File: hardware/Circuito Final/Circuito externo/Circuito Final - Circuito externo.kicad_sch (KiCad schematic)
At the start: 26 parts, among them J1 Conn_02x19_Odd_Even, J2 Conn_02x19_Odd_Even, J3 Conn_01x02, J4 Conn_01x02, SW1 SW_SPDT, SW2 SW_DIP_x04, U1 Opamp_Quad, U2 Opamp_Dual

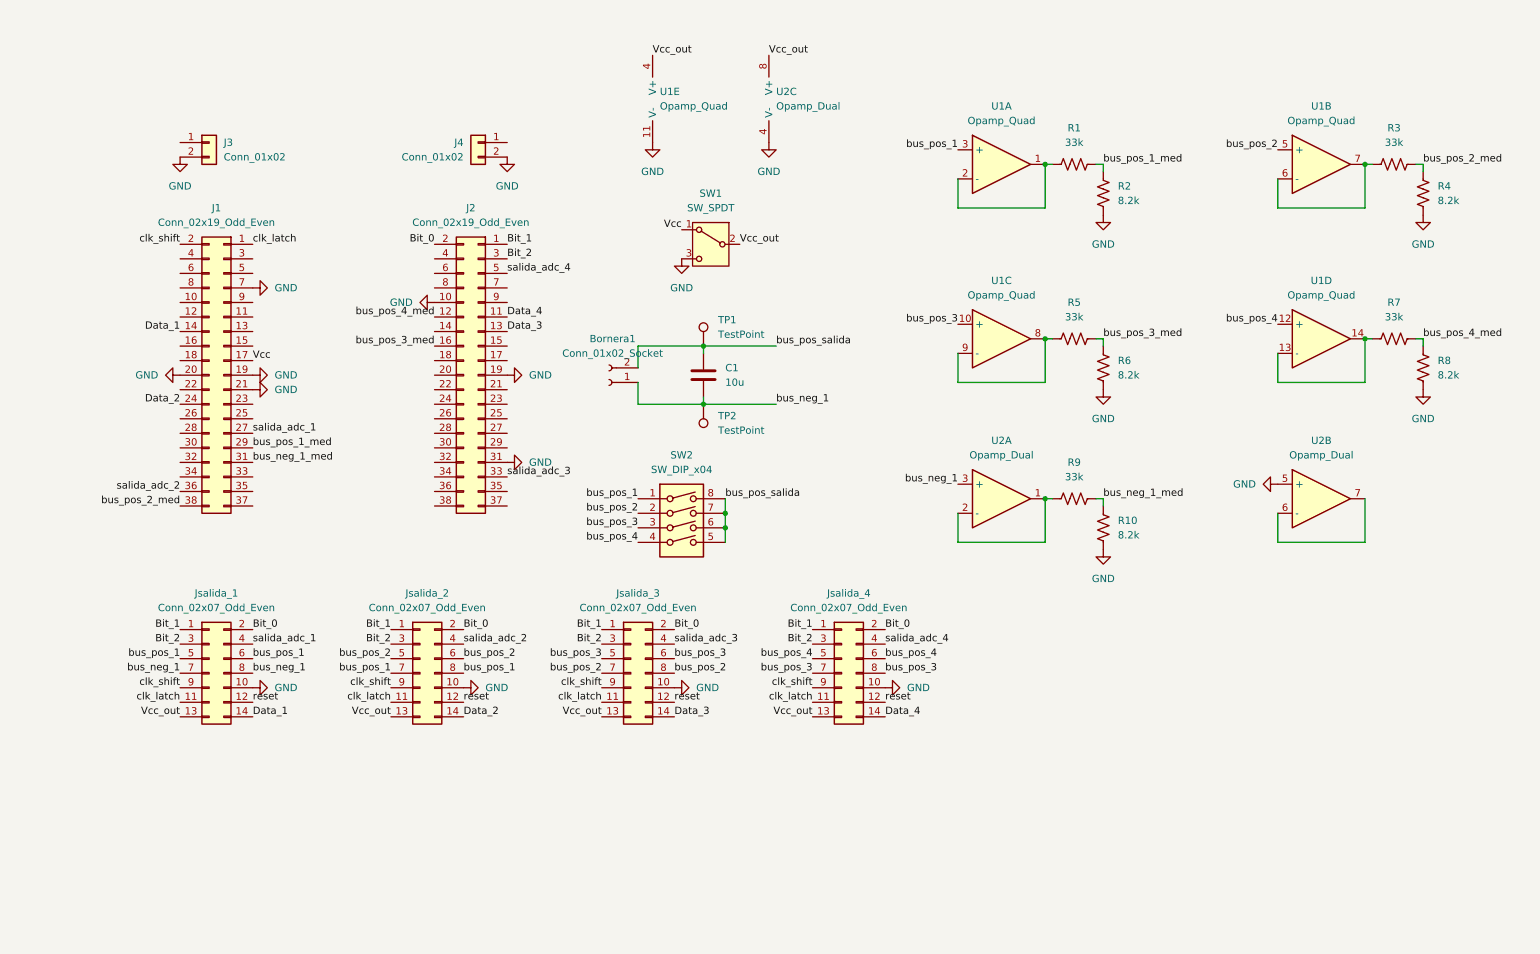
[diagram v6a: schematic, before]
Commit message: subida de la bitacora, del spice del sumador no inversor y update del kicad del circuito central
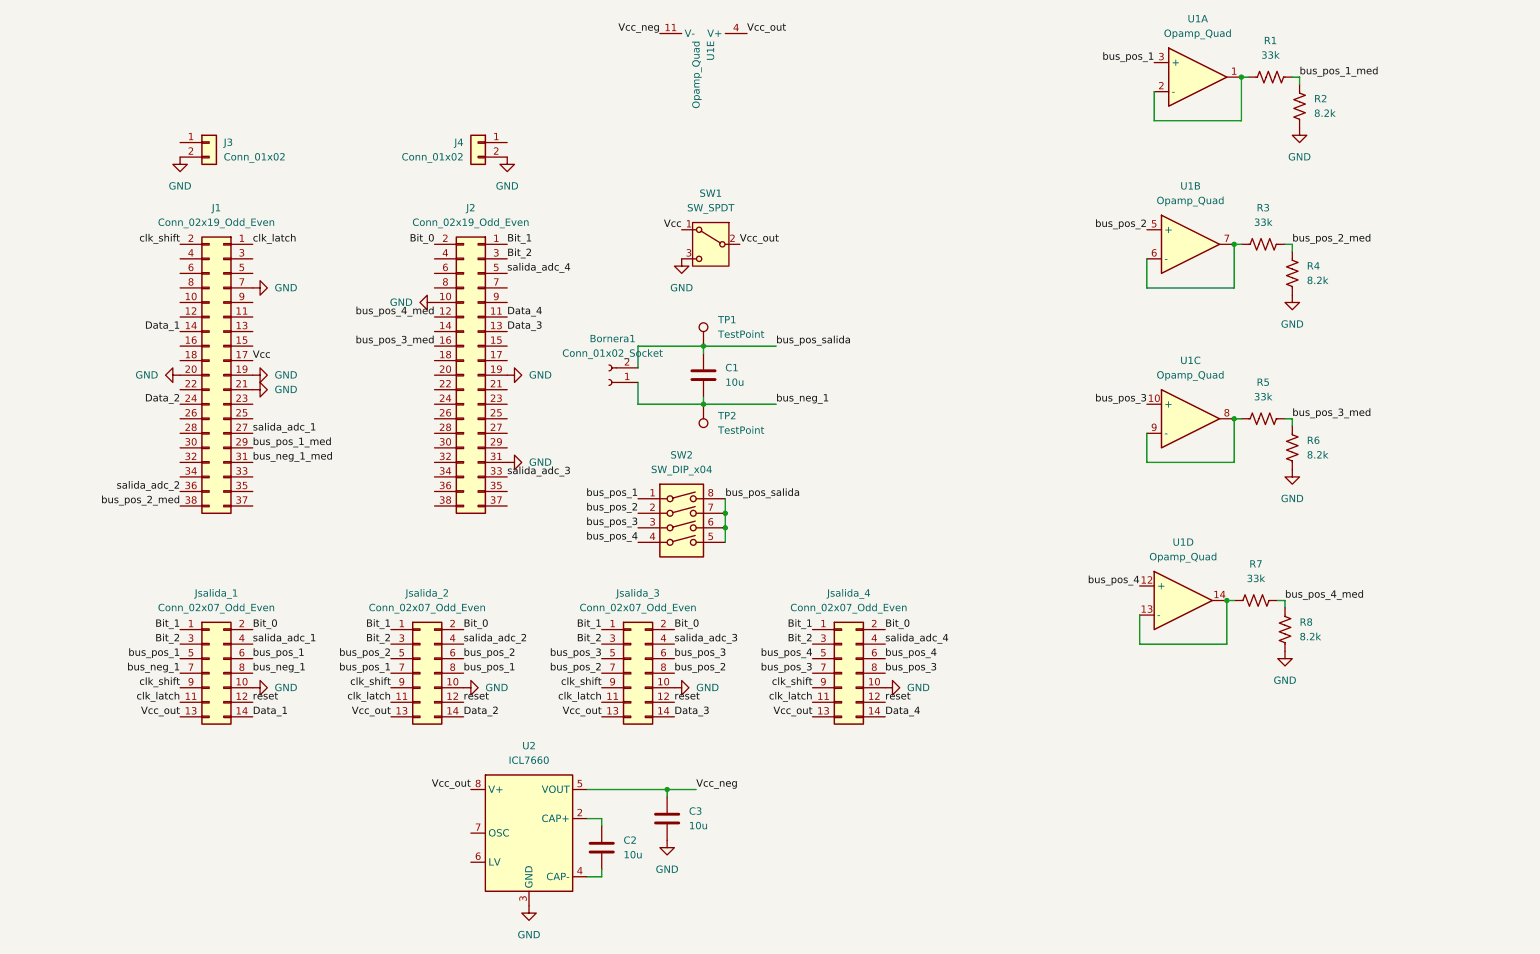
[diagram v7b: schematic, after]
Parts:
- removed R10: 8.2k, symbol Device:R_US
- removed R9: 33k, symbol Device:R_US
- removed U2: Opamp_Dual, symbol Device:Opamp_Dual
- added C2, C3: 10u, Capacitor_SMD:C_1206_3216Metric_Pad1.33x1.80mm_HandSolder, symbol Device:C
- added U2: ICL7660, Package_SO:SOIC-8_3.9x4.9mm_P1.27mm, symbol Regulator_SwitchedCapacitor:ICL7660
- R1, R2: footprint (none) -> Resistor_SMD:R_1206_3216Metric_Pad1.30x1.75mm_HandSolder
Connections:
- net GND: now also C3.2, U2.3 (GND); no longer U1.11 (V-)
- net Vcc_out: now also U2.8 (V+)
- new net: C2.1, U2.2 (CAP+)
- new net: C2.2, U2.4 (CAP-)
- new net Vcc_neg: C3.1, U1.11 (V-), U2.5 (VOUT)
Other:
- moved on the sheet: R1, R2, R3, R4, R5, R6, R7, R8, U1A, U1B, U1C, U1D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

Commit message: update del pcb del circuito central y subida de bitacora del 24 de junio
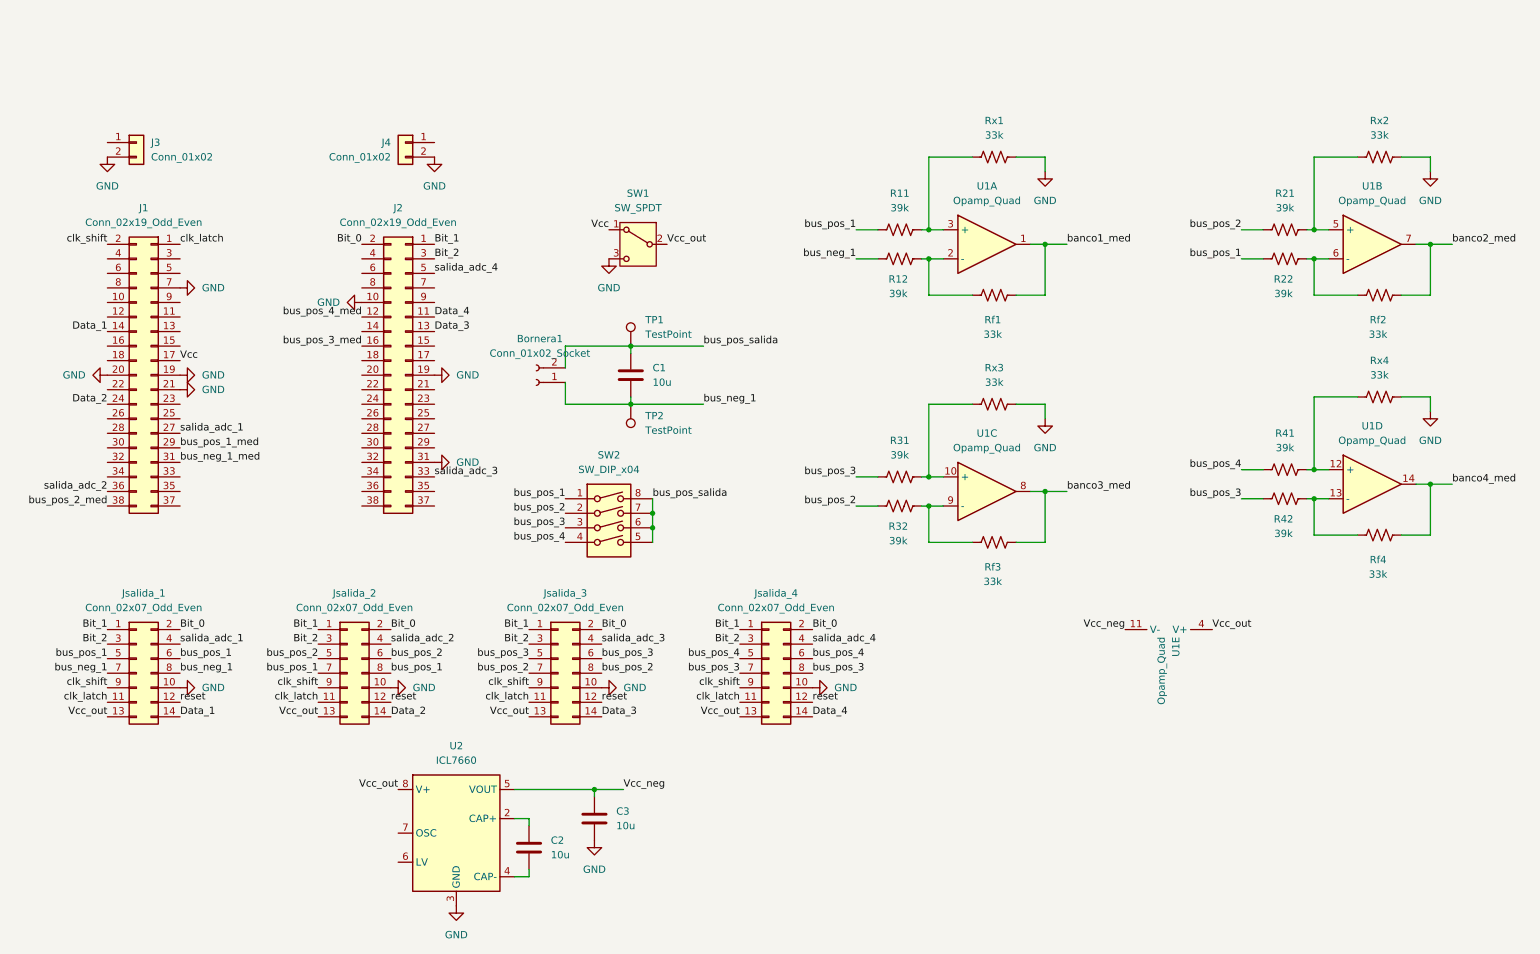
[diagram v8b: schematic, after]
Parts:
- removed R2: 8.2k, Resistor_SMD:R_1206_3216Metric_Pad1.30x1.75mm_HandSolder, symbol Device:R_US
- removed R3, R5, R7: 33k, symbol Device:R_US
- removed R4, R6, R8: 8.2k, symbol Device:R_US
- added R11, R12, R21, R22, R31, R32, R41, R42: 39k, Resistor_SMD:R_1206_3216Metric_Pad1.30x1.75mm_HandSolder, symbol Device:R_US
- added Rf1, Rf2, Rf3, Rf4, Rx2, Rx3, Rx4: 33k, Resistor_SMD:R_1206_3216Metric_Pad1.30x1.75mm_HandSolder, symbol Device:R_US
- U1: footprint (none) -> Package_SO:SO-14_3.9x8.65mm_P1.27mm
- renumbered R1 to Rx1
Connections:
- net GND: now also Rx1.2, Rx2.2, Rx3.2, Rx4.2
- net bus_neg_1: now also R12.2
- net bus_pos_1: now also R11.1, R22.2; no longer U1.3 (+)
- net bus_pos_1_med: no longer Rx1.2
- net bus_pos_2: now also R21.1, R32.2; no longer U1.5 (+)
- net bus_pos_3: now also R31.1, R42.2; no longer U1.10 (+)
- net bus_pos_4: now also R41.1; no longer U1.12 (+)
- net at U1.9 (-): now also R32.1, Rf3.1; no longer U1.8
- net at U1.6 (-): now also R22.1, Rf2.1; no longer U1.7
- net at U1.13 (-): now also R42.1, Rf4.1; no longer U1.14
- new net: R12.1, Rf1.1, U1.2 (-)
- new net: R31.2, Rx3.1, U1.10 (+)
- new net: R21.2, Rx2.1, U1.5 (+)
- new net: R11.2, Rx1.1, U1.3 (+)
- new net: R41.2, Rx4.1, U1.12 (+)
- new net banco1_med: Rf1.2, U1.1
- new net banco2_med: Rf2.2, U1.7
- new net banco3_med: Rf3.2, U1.8
- new net banco4_med: Rf4.2, U1.14
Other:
- moved on the sheet: Bornera1, C1, C2, C3, J1, J2, J3, J4, Jsalida_1, Jsalida_2, Jsalida_3, Jsalida_4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
